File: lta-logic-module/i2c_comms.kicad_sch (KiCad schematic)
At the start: 12 parts, among them U3 PCF8574, U4 PCF8574, U5 PCF8574

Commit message: Add light sensor circuit.
Adjust TODOs and comments after testing btn circuit.
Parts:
- C10, C11, C9: value 100n -> (none); footprint Capacitor_SMD:C_0603_1608Metric -> (none)
- C6, C7, C8: value 1u -> (none); footprint Capacitor_SMD:C_0603_1608Metric -> (none)
- R3, R4, R5: value 4K7 -> (none); footprint Resistor_SMD:R_0603_1608Metric -> (none)
- U3, U4, U5: value PCF8574 -> (none); footprint Aaron_TI_Parts:TI_SOIC_DW0016A -> (none)
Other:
- note added: "I2C Communication Bus Break-out"
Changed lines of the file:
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@@
     (effects (font (size 1.27 1.27)) (justify left bottom))
+  )
+  (text "I2C Communication Bus Break-out" (at 182.88 174.625 0)
+    (effects (font (size 2.54 2.54)) (justify left bottom))
   )
   (text "3V3 logic through I2C bus" (at 32.385 17.145 0)
@@
   (symbol (lib_id "power:GND") (at 92.71 104.775 0) (unit 1)
     (in_bom yes) (on_board yes) (fields_autoplaced)
-    (property "Reference" "#PWR027" (id 0) (at 92.71 111.125 0)
+    (property "Reference" "#PWR029" (id 0) (at 92.71 111.125 0)
       (effects (font (size 1.27 1.27)) hide)
     )
@@
   (symbol (lib_id "power:GND") (at 110.49 121.285 0) (unit 1)
     (in_bom yes) (on_board yes) (fields_autoplaced)
-    (property "Reference" "#PWR030" (id 0) (at 110.49 127.635 0)
+    (property "Reference" "#PWR032" (id 0) (at 110.49 127.635 0)
       (effects (font (size 1.27 1.27)) hide)
     )
@@
   (symbol (lib_id "power:GND") (at 110.49 173.355 0) (unit 1)
     (in_bom yes) (on_board yes) (fields_autoplaced)
-    (property "Reference" "#PWR031" (id 0) (at 110.49 179.705 0)
+    (property "Reference" "#PWR033" (id 0) (at 110.49 179.705 0)
       (effects (font (size 1.27 1.27)) hide)
     )
@@
       (effects (font (size 1.27 1.27)) (justify left))
     )
-    (property "Value" "4K7" (id 1) (at 77.0636 137.5922 0)
-      (effects (font (size 1.27 1.27)) (justify left))
-    )
-    (property "Footprint" "Resistor_SMD:R_0603_1608Metric" (id 2) (at 75.565 135.89 0)
+    (property "Value" "" (id 1) (at 77.0636 137.5922 0)
+      (effects (font (size 1.27 1.27)) (justify left))
+    )
+    (property "Footprint" "" (id 2) (at 75.565 135.89 0)
       (effects (font (size 1.27 1.27)) hide)
     )
@@
   (symbol (lib_id "power:GND") (at 92.71 154.94 270) (unit 1)
     (in_bom yes) (on_board yes)
-    (property "Reference" "#PWR028" (id 0) (at 86.36 154.94 0)
+    (property "Reference" "#PWR030" (id 0) (at 86.36 154.94 0)
       (effects (font (size 1.27 1.27)) hide)
     )
@@
       (effects (font (size 1.27 1.27)) (justify right))
     )
-    (property "Value" "100n" (id 1) (at 101.1809 132.5058 0)
-      (effects (font (size 1.27 1.27)) (justify right))
-    )
-    (property "Footprint" "Capacitor_SMD:C_0603_1608Metric" (id 2) (at 103.505 130.81 0)
+    (property "Value" "" (id 1) (at 101.1809 132.5058 0)
+      (effects (font (size 1.27 1.27)) (justify right))
+    )
+    (property "Footprint" "" (id 2) (at 103.505 130.81 0)
       (effects (font (size 1.27 1.27)) hide)
     )
@@
       (effects (font (size 1.27 1.27)) (justify left))
     )
-    (property "Value" "4K7" (id 1) (at 75.7936 158.5472 0)
-      (effects (font (size 1.27 1.27)) (justify left))
-    )
-    (property "Footprint" "Resistor_SMD:R_0603_1608Metric" (id 2) (at 74.295 156.845 0)
+    (property "Value" "" (id 1) (at 75.7936 158.5472 0)
+      (effects (font (size 1.27 1.27)) (justify left))
+    )
+    (property "Footprint" "" (id 2) (at 74.295 156.845 0)
       (effects (font (size 1.27 1.27)) hide)
     )
@@
   (symbol (lib_id "power:GND") (at 110.49 71.12 0) (unit 1)
     (in_bom yes) (on_board yes) (fields_autoplaced)
-    (property "Reference" "#PWR029" (id 0) (at 110.49 77.47 0)
+    (property "Reference" "#PWR031" (id 0) (at 110.49 77.47 0)
       (effects (font (size 1.27 1.27)) hide)
     )
@@
       (effects (font (size 1.27 1.27)) (justify right))
     )
-    (property "Value" "1u" (id 1) (at 87.2109 81.7058 0)
-      (effects (font (size 1.27 1.27)) (justify right))
-    )
-    (property "Footprint" "Capacitor_SMD:C_0603_1608Metric" (id 2) (at 89.535 80.01 0)
+    (property "Value" "" (id 1) (at 87.2109 81.7058 0)
+      (effects (font (size 1.27 1.27)) (justify right))
+    )
+    (property "Footprint" "" (id 2) (at 89.535 80.01 0)
       (effects (font (size 1.27 1.27)) hide)
     )
@@
   (symbol (lib_id "power:GND") (at 88.265 136.525 0) (unit 1)
     (in_bom yes) (on_board yes)
-    (property "Reference" "#PWR025" (id 0) (at 88.265 142.875 0)
+    (property "Reference" "#PWR027" (id 0) (at 88.265 142.875 0)
       (effects (font (size 1.27 1.27)) hide)
     )
@@
       (effects (font (size 1.27 1.27)) (justify right))
     )
-    (property "Value" "1u" (id 1) (at 91.0209 30.9058 0)
-      (effects (font (size 1.27 1.27)) (justify right))
-    )
-    (property "Footprint" "Capacitor_SMD:C_0603_1608Metric" (id 2) (at 93.345 29.21 0)
+    (property "Value" "" (id 1) (at 91.0209 30.9058 0)
+      (effects (font (size 1.27 1.27)) (justify right))
+    )
+    (property "Footprint" "" (id 2) (at 93.345 29.21 0)
       (effects (font (size 1.27 1.27)) hide)
     )
@@
       (effects (font (size 1.27 1.27)) (justify right))
     )
-    (property "Value" "100n" (id 1) (at 96.1009 81.7058 0)
-      (effects (font (size 1.27 1.27)) (justify right))
-    )
-    (property "Footprint" "Capacitor_SMD:C_0603_1608Metric" (id 2) (at 98.425 80.01 0)
+    (property "Value" "" (id 1) (at 96.1009 81.7058 0)
+      (effects (font (size 1.27 1.27)) (justify right))
+    )
+    (property "Footprint" "" (id 2) (at 98.425 80.01 0)
       (effects (font (size 1.27 1.27)) hide)
     )
@@
       (effects (font (size 1.27 1.27)) (justify right))
     )
-    (property "Value" "100n" (id 1) (at 99.9109 30.9058 0)
-      (effects (font (size 1.27 1.27)) (justify right))
-    )
-    (property "Footprint" "Capacitor_SMD:C_0603_1608Metric" (id 2) (at 102.235 29.21 0)
+    (property "Value" "" (id 1) (at 99.9109 30.9058 0)
+      (effects (font (size 1.27 1.27)) (justify right))
+    )
+    (property "Footprint" "" (id 2) (at 102.235 29.21 0)
       (effects (font (size 1.27 1.27)) hide)
     )
@@
   (symbol (lib_id "power:GND") (at 87.63 34.925 0) (unit 1)
     (in_bom yes) (on_board yes)
-    (property "Reference" "#PWR024" (id 0) (at 87.63 41.275 0)
+    (property "Reference" "#PWR026" (id 0) (at 87.63 41.275 0)
       (effects (font (size 1.27 1.27)) hide)
     )
@@
       (effects (font (size 1.27 1.27)) (justify left))
     )
-    (property "Value" "PCF8574" (id 1) (at 112.5094 84.5621 0)
-      (effects (font (size 1.27 1.27)) (justify left))
-    )
-    (property "Footprint" "Aaron_TI_Parts:TI_SOIC_DW0016A" (id 2) (at 110.49 100.965 0)
+    (property "Value" "" (id 1) (at 112.5094 84.5621 0)
+      (effects (font (size 1.27 1.27)) (justify left))
+    )
+    (property "Footprint" "" (id 2) (at 110.49 100.965 0)
       (effects (font (size 1.27 1.27)) hide)
     )
@@
   (symbol (lib_id "power:GND") (at 28.575 22.225 0) (unit 1)
     (in_bom yes) (on_board yes) (fields_autoplaced)
-    (property "Reference" "#PWR022" (id 0) (at 28.575 28.575 0)
+    (property "Reference" "#PWR024" (id 0) (at 28.575 28.575 0)
       (effects (font (size 1.27 1.27)) hide)
     )
@@
       (effects (font (size 1.27 1.27)) (justify left))
     )
-    (property "Value" "4K7" (id 1) (at 68.1736 137.5922 0)
-      (effects (font (size 1.27 1.27)) (justify left))
-    )
-    (property "Footprint" "Resistor_SMD:R_0603_1608Metric" (id 2) (at 66.675 135.89 0)
+    (property "Value" "" (id 1) (at 68.1736 137.5922 0)
+      (effects (font (size 1.27 1.27)) (justify left))
+    )
+    (property "Footprint" "" (id 2) (at 66.675 135.89 0)
       (effects (font (size 1.27 1.27)) hide)
     )
@@
   (symbol (lib_id "power:GND") (at 92.71 54.61 0) (unit 1)
     (in_bom yes) (on_board yes) (fields_autoplaced)
-    (property "Reference" "#PWR026" (id 0) (at 92.71 60.96 0)
+    (property "Reference" "#PWR028" (id 0) (at 92.71 60.96 0)
       (effects (font (size 1.27 1.27)) hide)
     )
@@
       (effects (font (size 1.27 1.27)) (justify left))
     )
-    (property "Value" "PCF8574" (id 1) (at 112.5094 34.3971 0)
-      (effects (font (size 1.27 1.27)) (justify left))
-    )
-    (property "Footprint" "Aaron_TI_Parts:TI_SOIC_DW0016A" (id 2) (at 110.49 50.8 0)
+    (property "Value" "" (id 1) (at 112.5094 34.3971 0)
+      (effects (font (size 1.27 1.27)) (justify left))
+    )
+    (property "Footprint" "" (id 2) (at 110.49 50.8 0)
       (effects (font (size 1.27 1.27)) hide)
     )
@@
   (symbol (lib_id "power:GND") (at 83.185 85.725 0) (unit 1)
     (in_bom yes) (on_board yes)
-    (property "Reference" "#PWR023" (id 0) (at 83.185 92.075 0)
+    (property "Reference" "#PWR025" (id 0) (at 83.185 92.075 0)
       (effects (font (size 1.27 1.27)) hide)
     )
@@
       (effects (font (size 1.27 1.27)) (justify right))
     )
-    (property "Value" "1u" (id 1) (at 92.2909 132.5058 0)
-      (effects (font (size 1.27 1.27)) (justify right))
-    )
-    (property "Footprint" "Capacitor_SMD:C_0603_1608Metric" (id 2) (at 94.615 130.81 0)
+    (property "Value" "" (id 1) (at 92.2909 132.5058 0)
+      (effects (font (size 1.27 1.27)) (justify right))
+    )
+    (property "Footprint" "" (id 2) (at 94.615 130.81 0)
       (effects (font (size 1.27 1.27)) hide)
     )
@@
       (effects (font (size 1.27 1.27)) (justify left))
     )
-    (property "Value" "PCF8574" (id 1) (at 112.5094 135.9971 0)
-      (effects (font (size 1.27 1.27)) (justify left))
-    )
-    (property "Footprint" "Aaron_TI_Parts:TI_SOIC_DW0016A" (id 2) (at 110.49 152.4 0)
-      (effects (font (size 1.27 1.27)) hide)
-    )
+    (property "Value" "" (id 1) (at 112.5094 135.9971 0)
+      (effects (font (size 1.27 1.27)) (justify left))
+    )
+    (property "Footprint" "" (id 2) (at 110.49 152.4 0)
+      (effects (font (size 1.27 1.27)) hide)
+    )

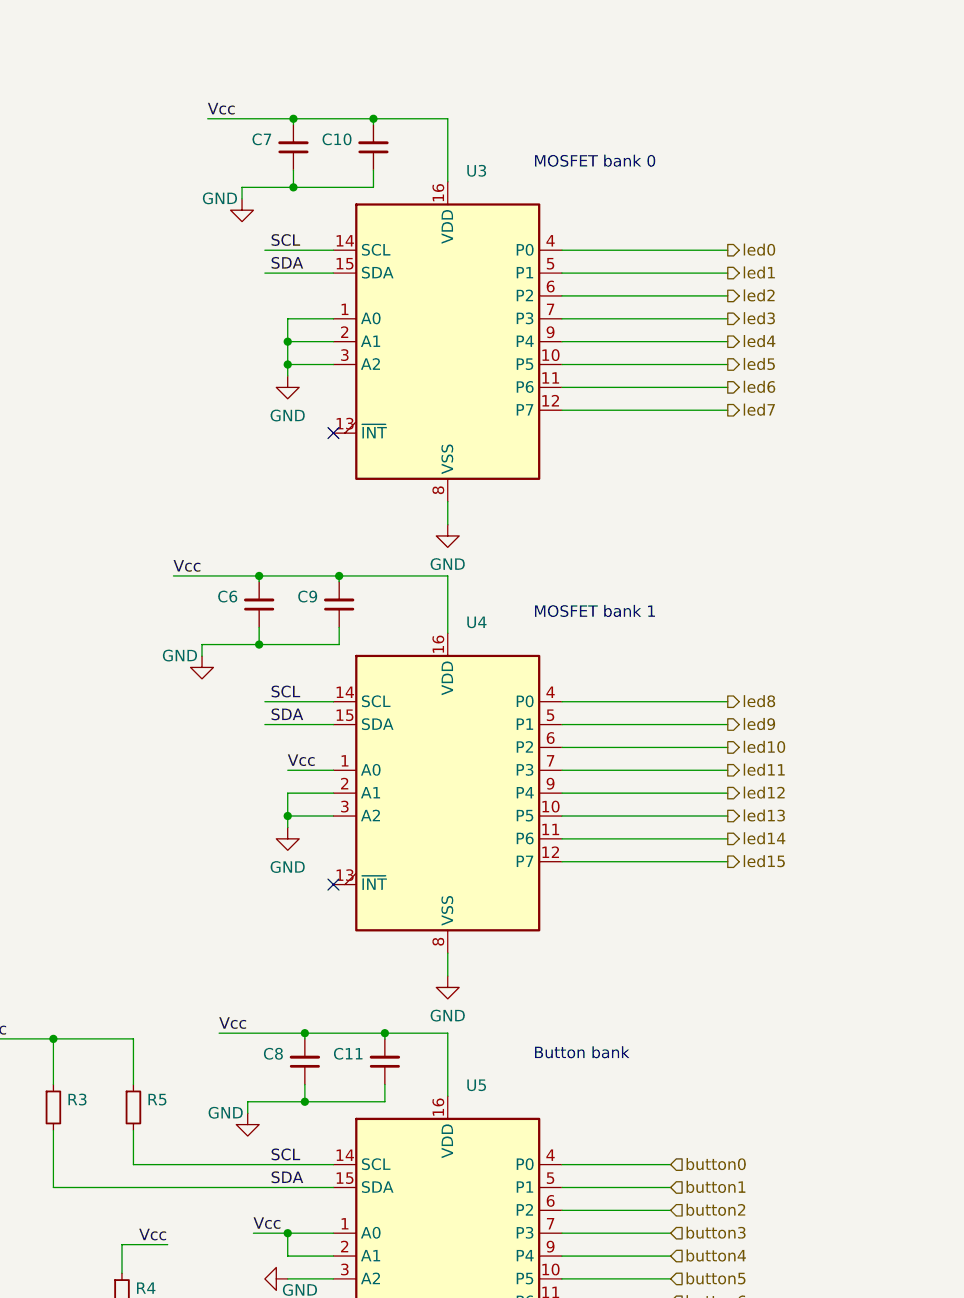
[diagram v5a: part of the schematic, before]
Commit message: Add main draft of PCB layout for logic module.
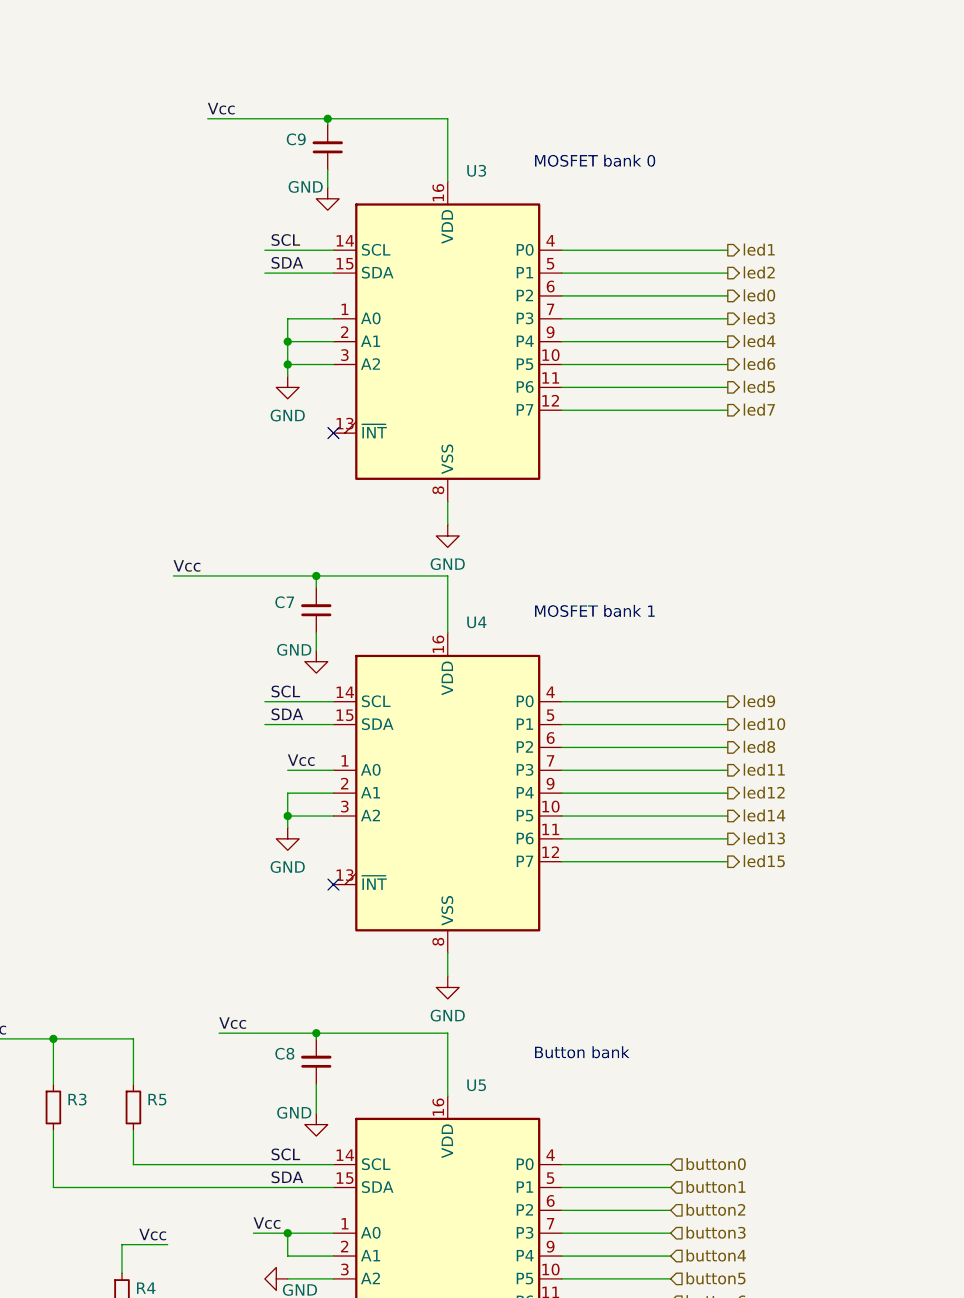
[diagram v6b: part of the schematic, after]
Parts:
- removed C6, C7, C8: (no value), symbol Device:C_Small
- U3, U4, U5: Comment (none) -> Exact MFR/MPN required
- renumbered C9 to C7, C11 to C8, C10 to C9
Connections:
- net led0: now also U3.6 (P2); no longer U3.4 (P0)
- net led1: now also U3.4 (P0); no longer U3.5 (P1)
- net led10: now also U4.5 (P1); no longer U4.6 (P2)
- net led13: now also U4.11 (P6); no longer U4.10 (P5)
- net led14: now also U4.10 (P5); no longer U4.11 (P6)
- net led2: now also U3.5 (P1); no longer U3.6 (P2)
- net led5: now also U3.11 (P6); no longer U3.10 (P5)
- net led6: now also U3.10 (P5); no longer U3.11 (P6)
- net led8: now also U4.6 (P2); no longer U4.4 (P0)
- net led9: now also U4.4 (P0); no longer U4.5 (P1)
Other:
- moved on the sheet: C7, C8, C9

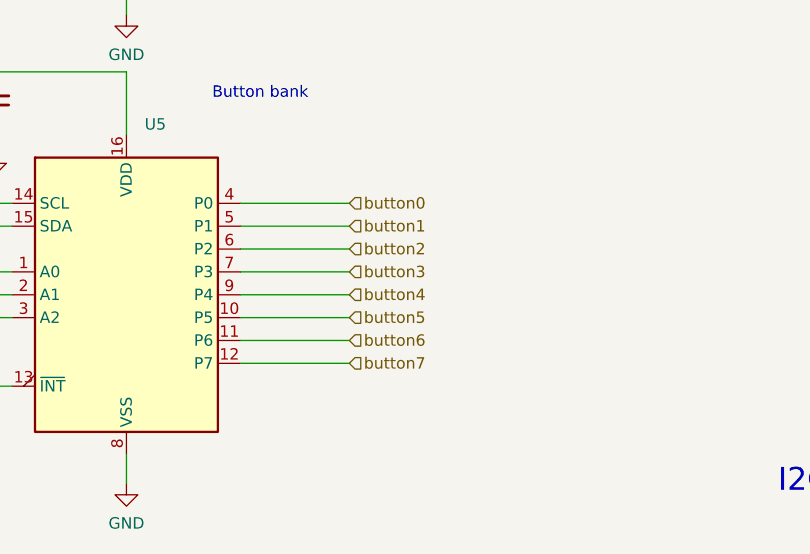
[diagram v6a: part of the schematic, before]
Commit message: Relocated optosensor to south side of board.
* Moved optosensor logic away from the USB plug-side of the Feather.
  You can now plug in USB while the Feather is attached to the board.
* Changed schematic such that `button0` now goes directly to the
  Feather; buttons 1--8 are on the I2C bus. Cleans up some obnoxious
  routing.
* Optimized other routing & GND fill.
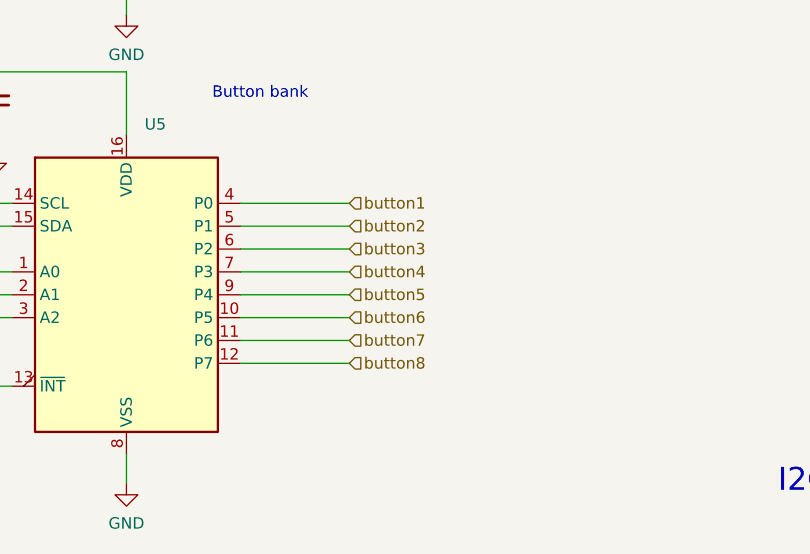
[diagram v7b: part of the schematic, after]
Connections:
- net button0 is gone; now on net button1: U5.4 (P0)
- net button1: no longer U5.5 (P1)
- net button2: now also U5.5 (P1); no longer U5.6 (P2)
- net button3: now also U5.6 (P2); no longer U5.7 (P3)
- net button4: now also U5.7 (P3); no longer U5.9 (P4)
- net button5: now also U5.9 (P4); no longer U5.10 (P5)
- net button6: now also U5.10 (P5); no longer U5.11 (P6)
- net button7: now also U5.11 (P6); no longer U5.12 (P7)
- new net button8: U5.12 (P7)
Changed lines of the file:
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@@
     (effects (font (size 1.27 1.27)) (justify left))
   )
-  (hierarchical_label "button2" (shape input) (at 135.255 147.32 0)
+  (hierarchical_label "button2" (shape input) (at 135.255 144.78 0)
     (effects (font (size 1.27 1.27)) (justify left))
   )
-  (hierarchical_label "button0" (shape input) (at 135.255 142.24 0)
+  (hierarchical_label "button8" (shape input) (at 135.255 160.02 0)
     (effects (font (size 1.27 1.27)) (justify left))
   )
@@
     (effects (font (size 1.27 1.27)) (justify left))
   )
-  (hierarchical_label "button6" (shape input) (at 135.255 157.48 0)
+  (hierarchical_label "button6" (shape input) (at 135.255 154.94 0)
     (effects (font (size 1.27 1.27)) (justify left))
   )
-  (hierarchical_label "button4" (shape input) (at 135.255 152.4 0)
+  (hierarchical_label "button4" (shape input) (at 135.255 149.86 0)
     (effects (font (size 1.27 1.27)) (justify left))
   )
@@
     (effects (font (size 1.27 1.27)) (justify left))
   )
-  (hierarchical_label "button3" (shape input) (at 135.255 149.86 0)
+  (hierarchical_label "button3" (shape input) (at 135.255 147.32 0)
     (effects (font (size 1.27 1.27)) (justify left))
   )
@@
     (effects (font (size 1.27 1.27)) (justify left))
   )
-  (hierarchical_label "button1" (shape input) (at 135.255 144.78 0)
+  (hierarchical_label "button1" (shape input) (at 135.255 142.24 0)
     (effects (font (size 1.27 1.27)) (justify left))
   )
-  (hierarchical_label "button5" (shape input) (at 135.255 154.94 0)
+  (hierarchical_label "button5" (shape input) (at 135.255 152.4 0)
     (effects (font (size 1.27 1.27)) (justify left))
   )
@@
     (effects (font (size 1.27 1.27)) (justify left))
   )
-  (hierarchical_label "button7" (shape input) (at 135.255 160.02 0)
+  (hierarchical_label "button7" (shape input) (at 135.255 157.48 0)
     (effects (font (size 1.27 1.27)) (justify left))
   )
